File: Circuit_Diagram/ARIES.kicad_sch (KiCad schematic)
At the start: 7 parts, among them M1 Motor_Servo, M2 Motor_Servo, M3 Motor_Servo, M4 Motor_Servo, M5 Motor_Servo, M6 End_Effector

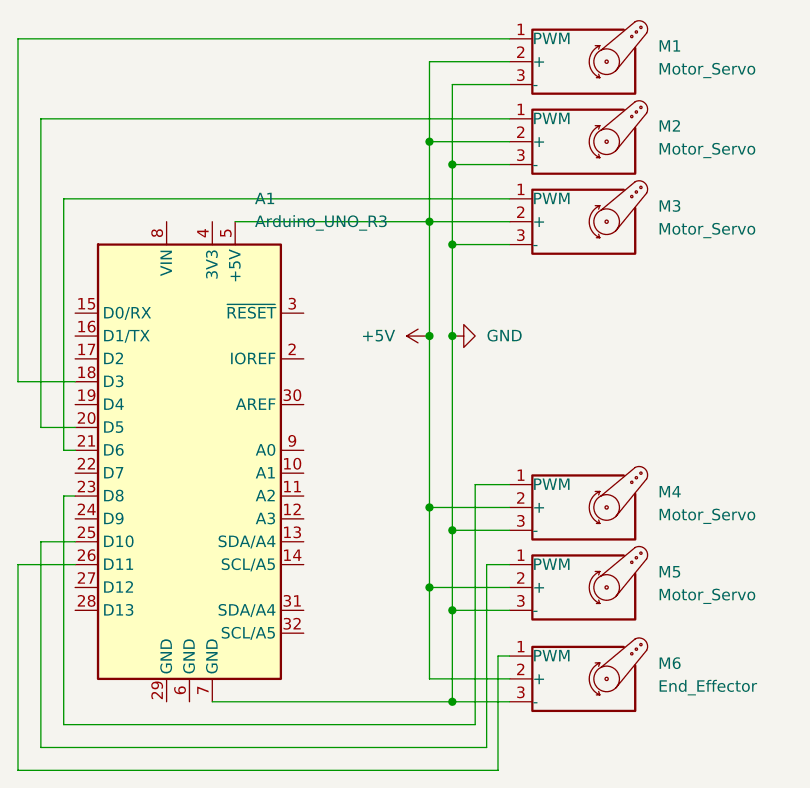
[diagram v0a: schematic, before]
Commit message: Refined Upload
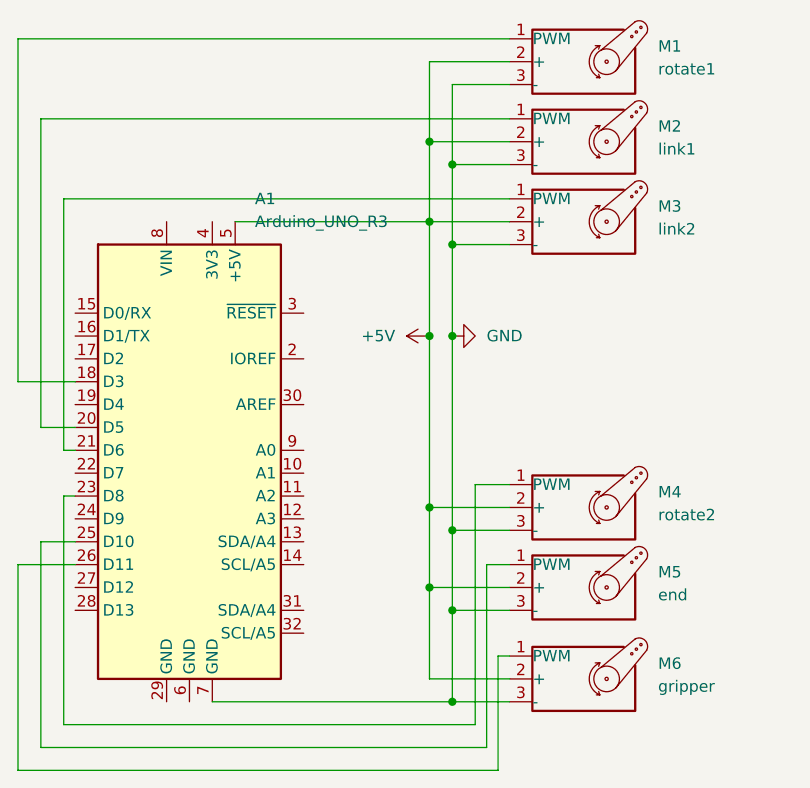
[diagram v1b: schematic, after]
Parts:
- M1: value Motor_Servo -> rotate1
- M2: value Motor_Servo -> link1
- M3: value Motor_Servo -> link2
- M4: value Motor_Servo -> rotate2
- M5: value Motor_Servo -> end
- M6: value End_Effector -> gripper
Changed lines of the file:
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@@
       (effects (font (size 1.27 1.27)) (justify left))
     )
-    (property "Value" "Motor_Servo" (at 179.07 104.9766 0)
+    (property "Value" "rotate2" (at 179.07 104.9766 0)
       (effects (font (size 1.27 1.27)) (justify left))
     )
@@
       (effects (font (size 1.27 1.27)) (justify left))
     )
-    (property "Value" "Motor_Servo" (at 179.07 73.2266 0)
+    (property "Value" "link2" (at 179.07 73.2266 0)
       (effects (font (size 1.27 1.27)) (justify left))
     )
@@
       (effects (font (size 1.27 1.27)) (justify left))
     )
-    (property "Value" "Motor_Servo" (at 179.07 55.4466 0)
+    (property "Value" "rotate1" (at 179.07 55.4466 0)
       (effects (font (size 1.27 1.27)) (justify left))
     )
@@
       (effects (font (size 1.27 1.27)) (justify left))
     )
-    (property "Value" "Motor_Servo" (at 179.07 113.8666 0)
+    (property "Value" "end" (at 179.07 113.8666 0)
       (effects (font (size 1.27 1.27)) (justify left))
     )
@@
       (effects (font (size 1.27 1.27)) (justify left))
     )
-    (property "Value" "End_Effector" (at 179.07 124.0266 0)
+    (property "Value" "gripper" (at 179.07 124.0266 0)
       (effects (font (size 1.27 1.27)) (justify left))
     )
@@
       (effects (font (size 1.27 1.27)) (justify left))
     )
-    (property "Value" "Motor_Servo" (at 179.07 64.3366 0)
+    (property "Value" "link1" (at 179.07 64.3366 0)
       (effects (font (size 1.27 1.27)) (justify left))
     )
